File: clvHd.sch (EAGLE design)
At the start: 44 parts, among them U1 ADS1293CISQ/NOPB, X1 BM02B-SRSS-TB, X2 BM07B-SRSS-TB, X3 BM07B-SRSS-TB

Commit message: finished
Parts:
- removed TP21: PTR1PAD1-17, testpad:PTR1PAD1-17
- renumbered LED1 to L1, LED2 to L2
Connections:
- net N$1: no longer S1.1

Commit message: panelization
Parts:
- C10, C9: value 4.70nF -> 22pF
- C11: value 4.70nF -> 1nF
- C12, C13, C16, C19: value 4.70nF -> 100nF
- C20: value 4.70nF -> 1000nF
- R11, R13: value 51 -> 1M
- R12, R7: value 51 -> 400
- R14: value 51 -> 10k
- R15: value 51 -> 10M
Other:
- moved on the sheet: C11, C19, C9, R14, R15, X1, X2, X3

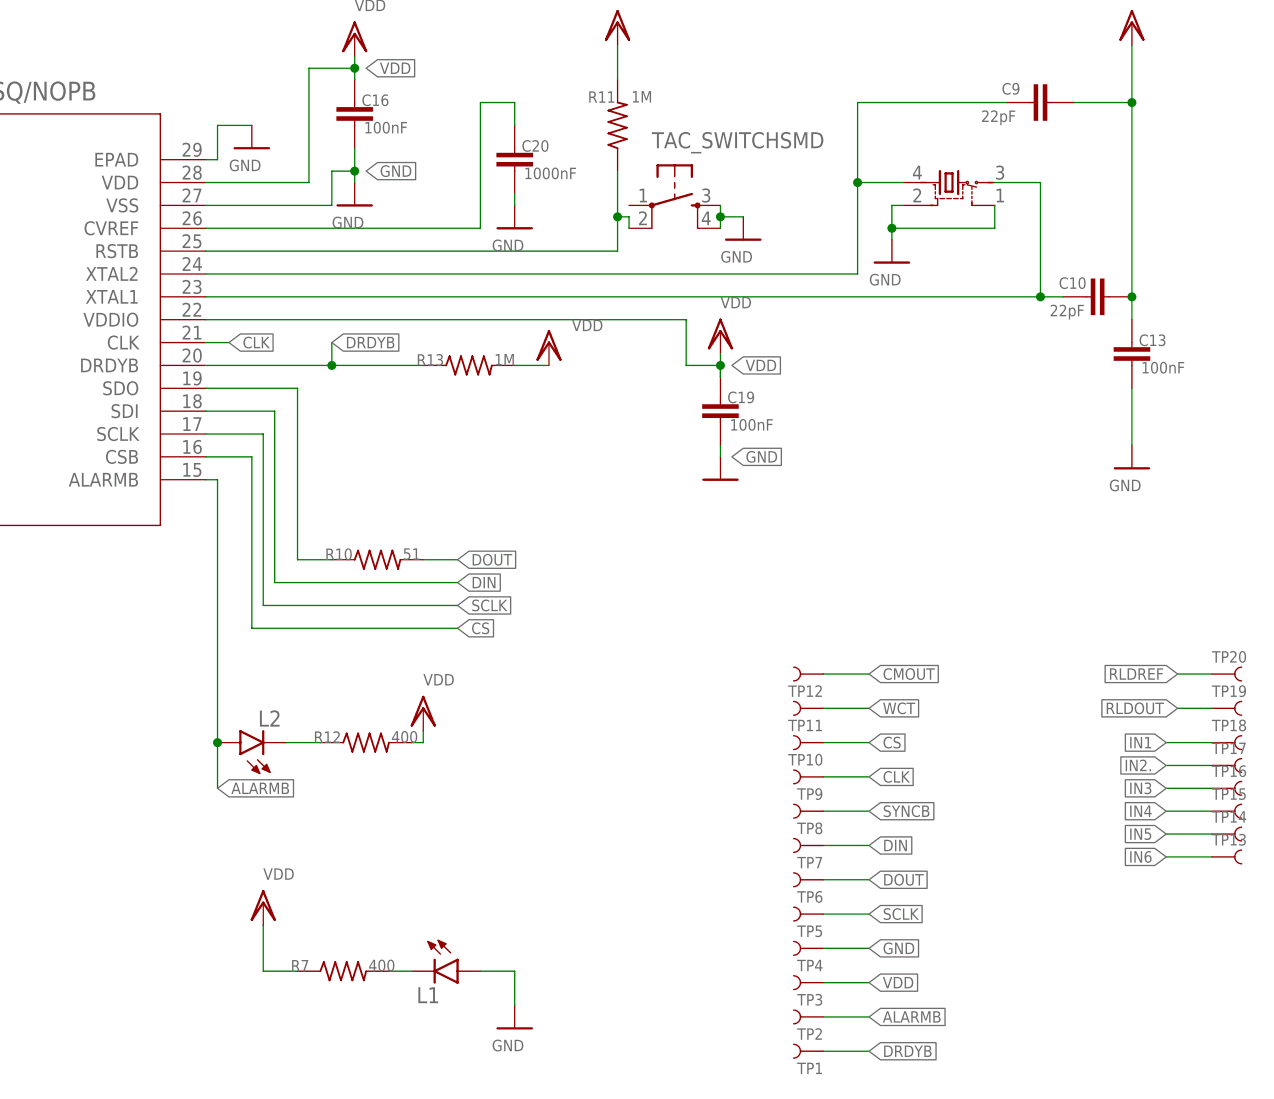
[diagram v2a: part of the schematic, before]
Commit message: component val + minor debug
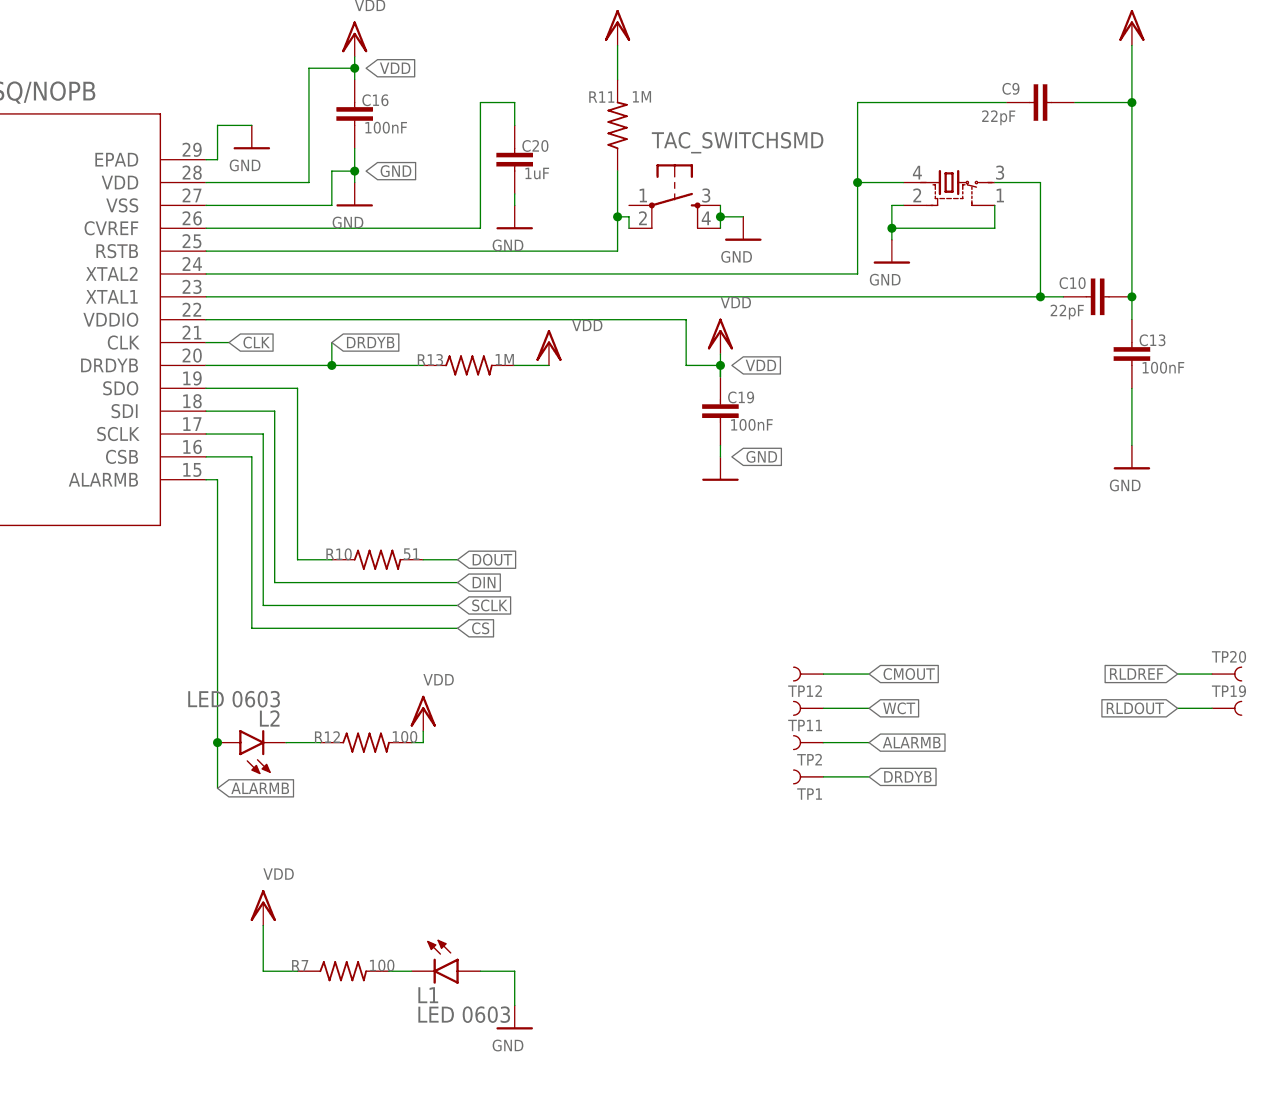
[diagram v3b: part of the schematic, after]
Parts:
- removed TP10, TP13, TP14, TP15, TP16, TP17, TP18, TP3, TP4, TP5, TP6, TP7, TP8, TP9: TEST-POINT3, SparkFun-Connectors:TEST-POINT3
- C11, C13, C16, C19, C9: device rcl:C-EUC0201 -> rcl:C-EUC0402
- C20: value 1000nF -> 1uF; device rcl:C-EUC0201 -> rcl:C-EUC0402
- L1, L2: value (none) -> LED 0603
- R10, R11, R14, R15: device rcl:R-US_R0201 -> rcl:R-US_R0402
- R12, R7: value 400 -> 100; device rcl:R-US_R0201 -> rcl:R-US_R0402
- U$1: value ASE -> C387328; device crystalCustom:ASE -> crystalCustom:C387328
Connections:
- net CLK: no longer TP9.1
- net CS: no longer TP10.1
- net DIN: no longer TP7.1
- net DOUT: no longer TP6.1
- net GND: no longer TP4.1
- net IN1: no longer TP18.1
- net IN2.: no longer TP17.1
- net IN3: no longer TP16.1
- net IN4: no longer TP15.1
- net IN5: no longer TP14.1
- net IN6: no longer TP13.1
- net SCLK: no longer TP5.1
- net SYNCB: no longer TP8.1
- net VDD: no longer TP3.1
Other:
- moved on the sheet: TP1, TP2
